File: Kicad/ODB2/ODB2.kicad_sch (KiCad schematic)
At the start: 32 parts, among them U1 STM32F412ZGTx

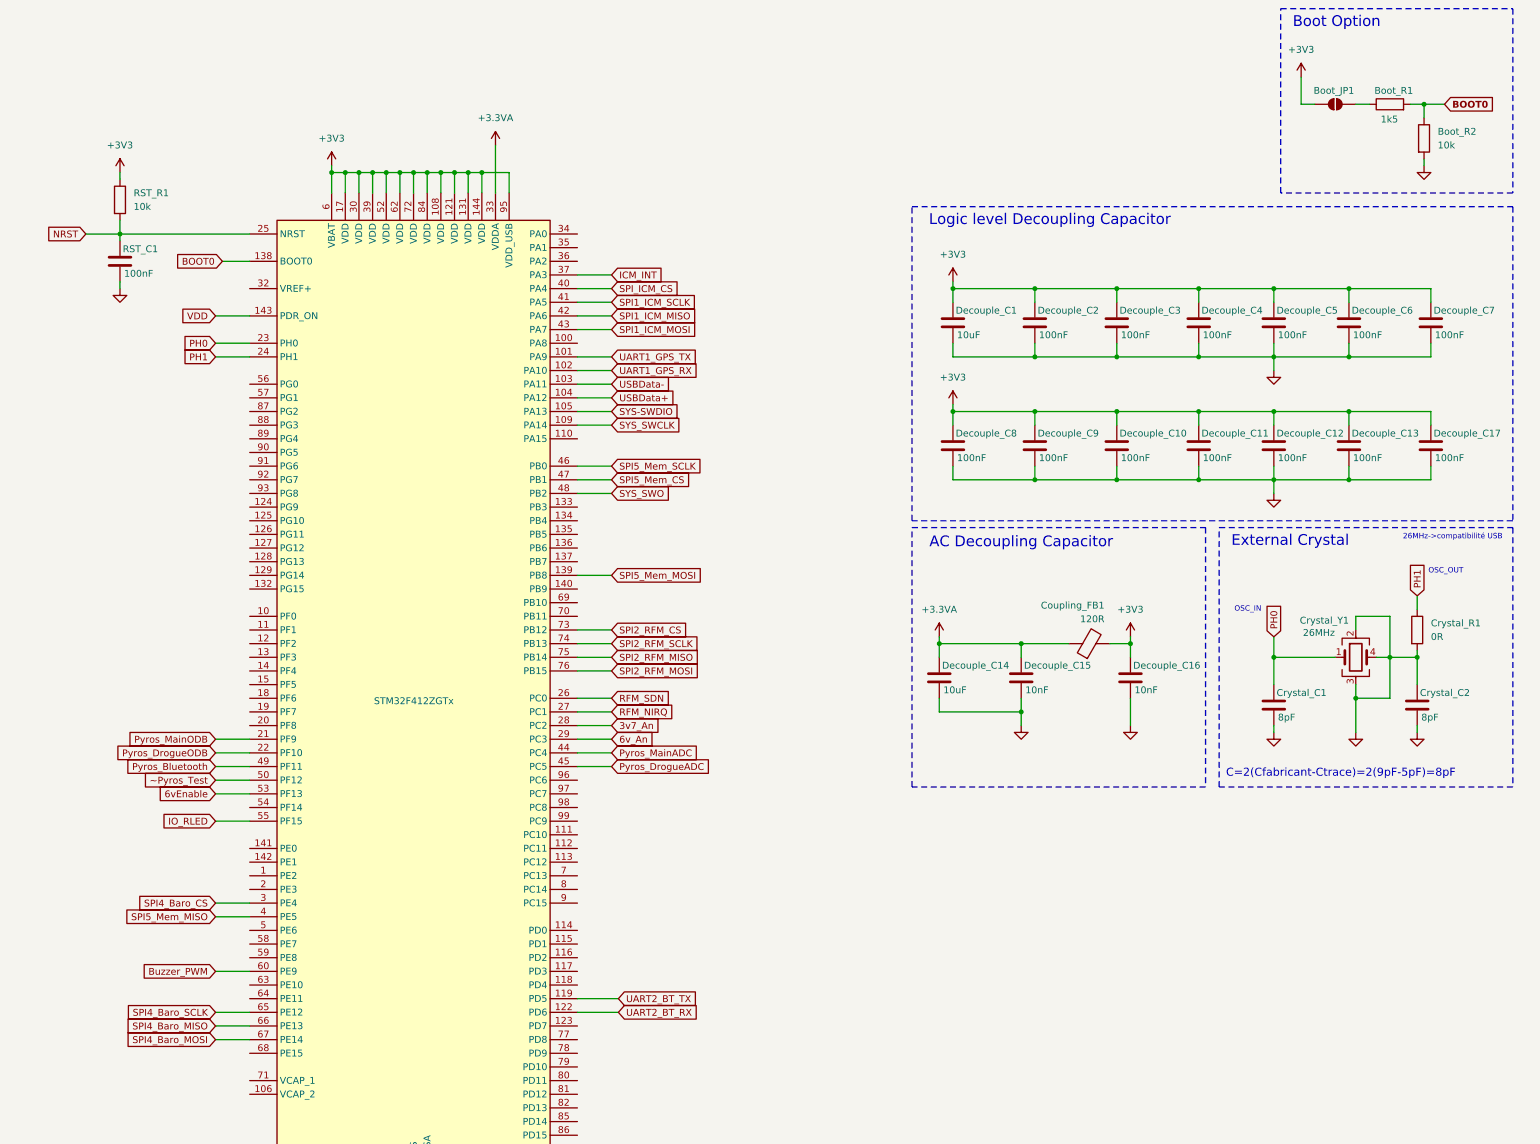
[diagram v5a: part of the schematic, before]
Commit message: fix sw0 + merge acc/rfm + fix pdr_on
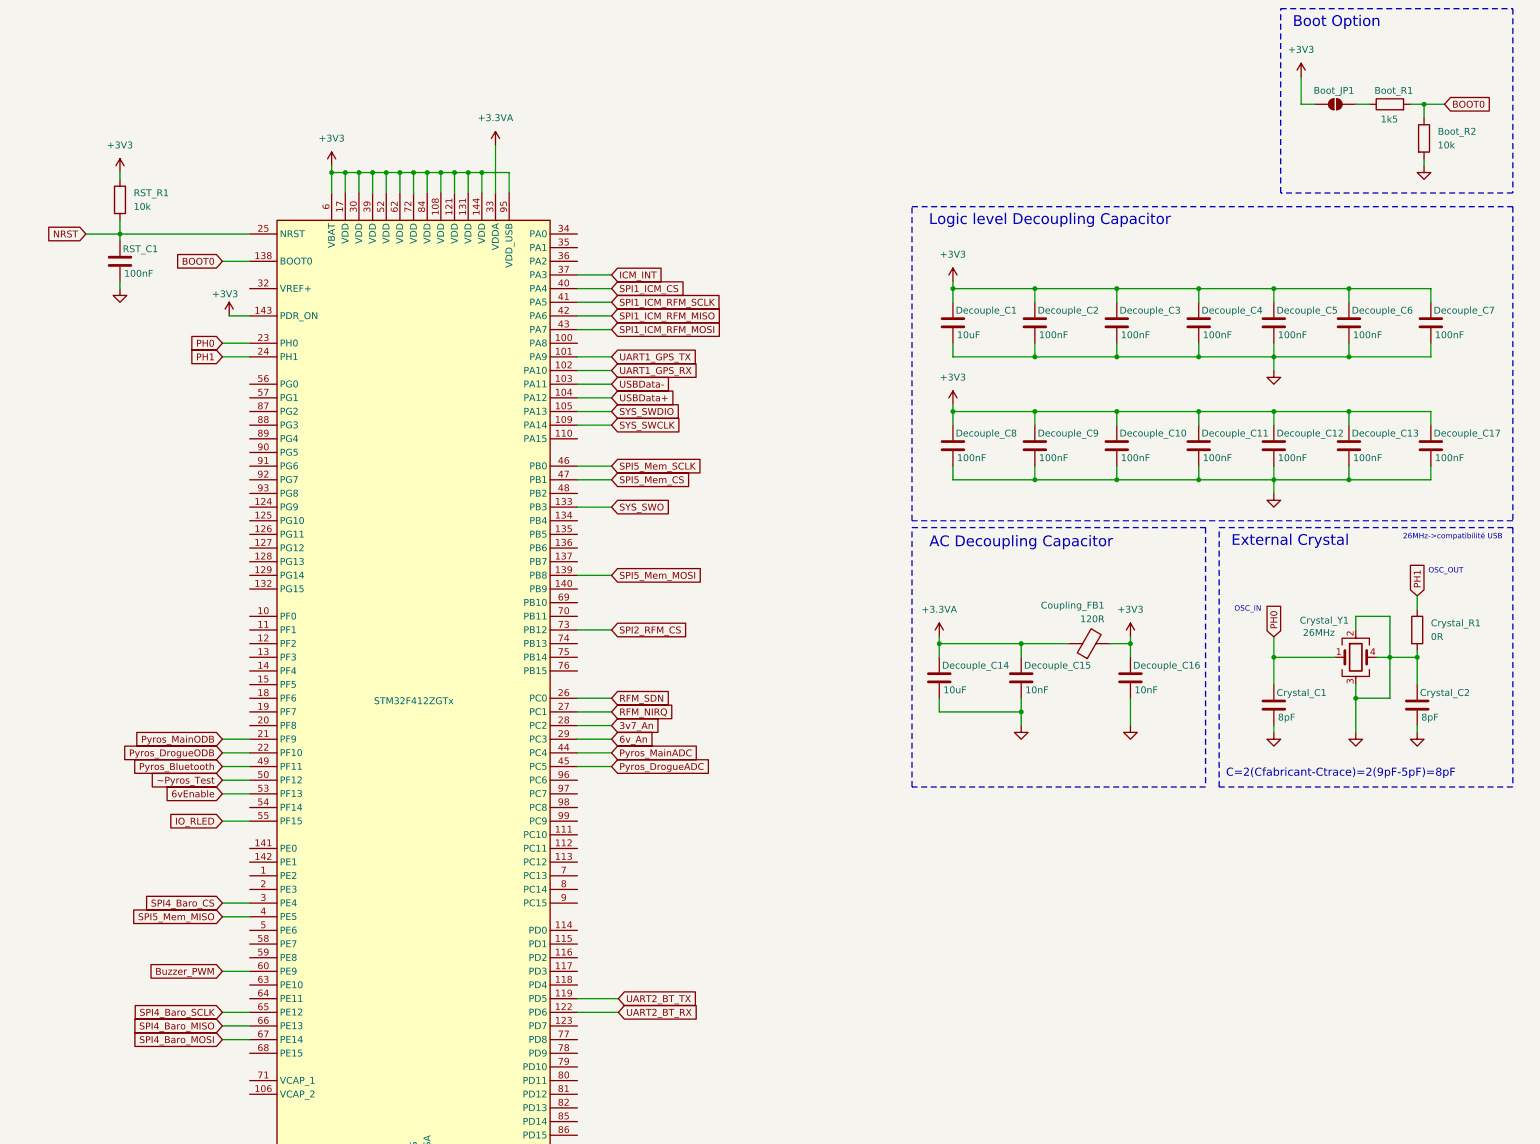
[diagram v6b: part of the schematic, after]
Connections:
- net VDD is gone; now on net +3V3: U1.143 (PDR_ON)
- net SYS_SWO: now also U1.133 (PB3); no longer U1.48 (PB2)
- net SPI1_ICM_MISO renamed SPI1_ICM_RFM_MISO
- net SPI1_ICM_MOSI renamed SPI1_ICM_RFM_MOSI
- net SPI1_ICM_SCLK renamed SPI1_ICM_RFM_SCLK
- net SPI2_RFM_MISO: no longer names the net of U1.75 (PB14)
- net SPI2_RFM_MOSI: no longer names the net of U1.76 (PB15)
- net SPI2_RFM_SCLK: no longer names the net of U1.74 (PB13)
- net SPI_ICM_CS renamed SPI1_ICM_CS
- net SYS-SWDIO renamed SYS_SWDIO

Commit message: rename rLED
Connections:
- net IO_RLED renamed IO_CriticalLED
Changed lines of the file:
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@@
 		)
 	)
-	(global_label "IO_RLED"
+	(global_label "IO_CriticalLED"
 		(shape input)
 		(at 165.1 165.1 180)
@@
 		)
 		(property "Intersheetrefs" "${INTERSHEET_REFS}"
-			(at 154.4948 165.1 0)
+			(at 148.8705 165.1 0)
 			(effects
 				(font

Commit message: fix RFM_CS
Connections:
- net SPI2_RFM_CS: now also U1.140 (PB9); no longer U1.73 (PB12)
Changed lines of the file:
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@@
 	(wire
 		(pts
-			(xy 231.14 200.66) (xy 238.76 200.66)
+			(xy 231.14 200.66) (xy 237.49 200.66)
 		)
 		(stroke
@@
 	(wire
 		(pts
+			(xy 231.14 121.92) (xy 237.49 121.92)
+		)
+		(stroke
+			(width 0)
+			(type default)
+		)
+	)
+	(wire
+		(pts
 			(xy 388.62 41.91) (xy 388.62 43.18)
 		)
@@
 	(wire
 		(pts
-			(xy 231.14 198.12) (xy 238.76 198.12)
+			(xy 231.14 198.12) (xy 237.49 198.12)
 		)
 		(stroke
@@
 		(pts
 			(xy 231.14 73.66) (xy 237.49 73.66)
-		)
-		(stroke
-			(width 0)
-			(type default)
-		)
-	)
-	(wire
-		(pts
-			(xy 231.14 129.54) (xy 237.49 129.54)
 		)
 		(stroke
@@
 	(global_label "UART2_BT_RX"
 		(shape input)
-		(at 238.76 200.66 0)
+		(at 237.49 200.66 0)
 		(fields_autoplaced yes)
 		(effects
@@
 		)
 		(property "Intersheetrefs" "${INTERSHEET_REFS}"
-			(at 254.2637 200.66 0)
+			(at 252.9937 200.66 0)
 			(effects
 				(font
@@
 	(global_label "UART2_BT_TX"
 		(shape input)
-		(at 238.76 198.12 0)
+		(at 237.49 198.12 0)
 		(fields_autoplaced yes)
 		(effects
@@
 		)
 		(property "Intersheetrefs" "${INTERSHEET_REFS}"
-			(at 253.9613 198.12 0)
+			(at 252.6913 198.12 0)
 			(effects
 				(font
@@
 	(global_label "SPI2_RFM_CS"
 		(shape input)
-		(at 237.49 129.54 0)
+		(at 237.49 121.92 0)
 		(fields_autoplaced yes)
 		(effects
@@
 		)
 		(property "Intersheetrefs" "${INTERSHEET_REFS}"
-			(at 252.9937 129.54 0)
-			(effects
-				(font
+			(at 252.9937 121.92 0)
+			(effects
+				(font
